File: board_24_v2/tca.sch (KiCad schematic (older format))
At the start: 26 parts, among them IC1 ATMEGA328-A, P1 CONN_2, P2 CONN_3X2, U1 SD_CARD, U2 LD1117S33, Y1 RESONATEUR

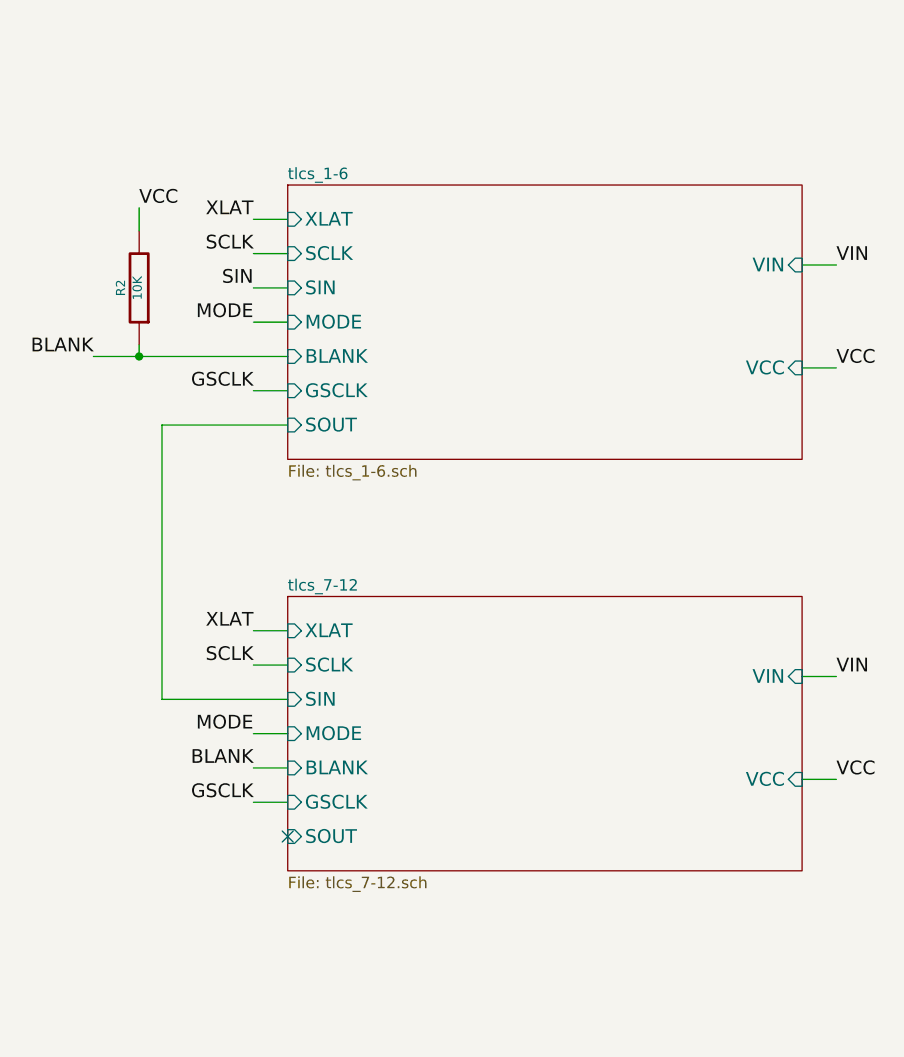
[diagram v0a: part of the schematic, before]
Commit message: Made board_24_v2 which uses PCB-mounted LED sockets and updated various issues on board_96 as well. These PCBs were ordered around 7/1/14.
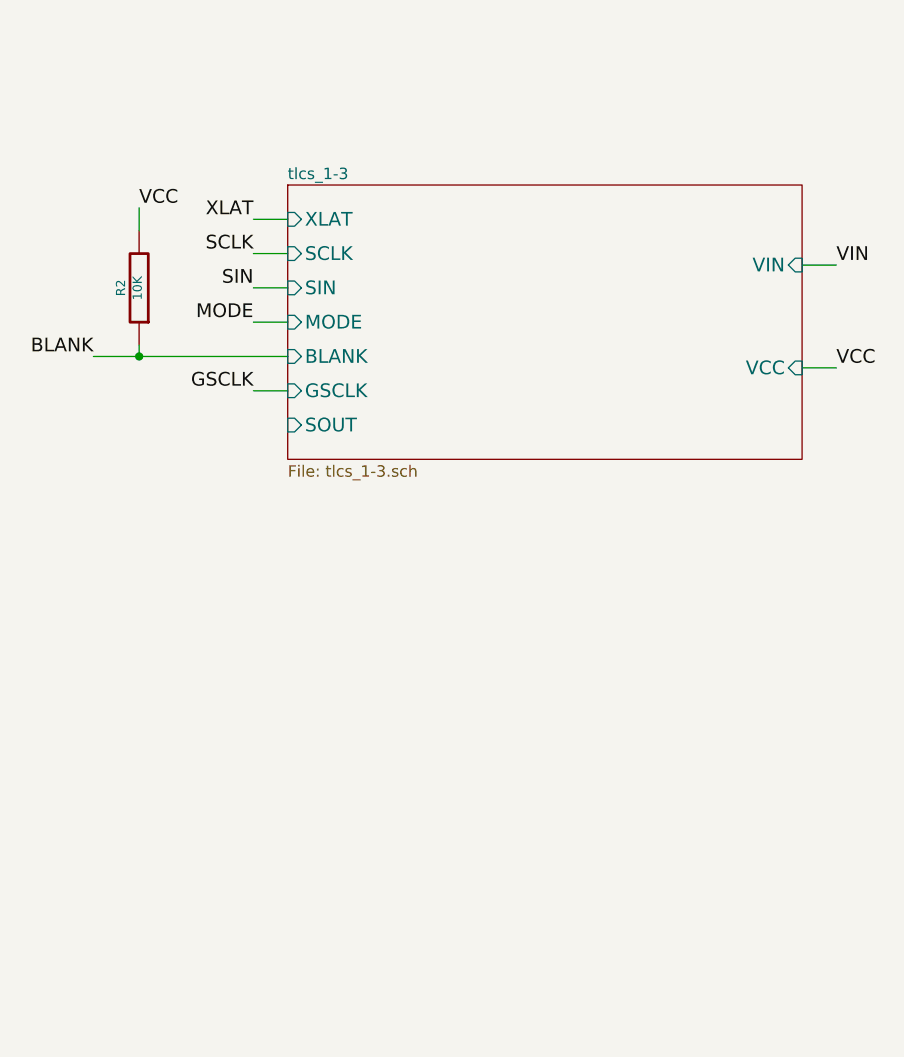
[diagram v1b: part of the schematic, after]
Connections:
- no-connect marks 11 -> 10
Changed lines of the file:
@@
 $Descr USLetter 11000 8500
 encoding utf-8
-Sheet 1 3
+Sheet 1 2
 Title ""
-Date "25 jun 2014"
+Date "27 jun 2014"
 Rev ""
 Comp ""
@@
 S 6800 2450 2250 1200
 U 5362FF20
-F0 "tlcs_1-6" 50
-F1 "tlcs_1-6.sch" 50
+F0 "tlcs_1-3" 50
+F1 "tlcs_1-3.sch" 50
 F2 "XLAT" I L 6800 2600 60
 F3 "SCLK" I L 6800 2750 60
@@
 Text Label 5950 3200 2    60   ~ 0
 BLANK
-Text Label 6650 4400 2    60   ~ 0
-XLAT
-Text Label 6650 4550 2    60   ~ 0
-SCLK
-Text Label 6650 4850 2    60   ~ 0
-MODE
-Text Label 6650 5150 2    60   ~ 0
-GSCLK
-Text Label 9200 4600 0    60   ~ 0
-VIN
-Text Label 9200 5050 0    60   ~ 0
-VCC
-Text Label 6650 5000 2    60   ~ 0
-BLANK
-NoConn ~ 6800 5300
-$Sheet
-S 6800 4250 2250 1200
-U 53633D51
-F0 "tlcs_7-12" 50
-F1 "tlcs_7-12.sch" 50
-F2 "XLAT" I L 6800 4400 60
-F3 "SCLK" I L 6800 4550 60
-F4 "SIN" I L 6800 4700 60
-F5 "MODE" I L 6800 4850 60
-F6 "BLANK" I L 6800 5000 60
-F7 "GSCLK" I L 6800 5150 60
-F8 "VIN" I R 9050 4600 60
-F9 "VCC" I R 9050 5050 60
-F10 "SOUT" I L 6800 5300 60
-$EndSheet
 $Comp
 L INDUCTOR L1
@@
 	9050 3250 9200 3250
 Wire Wire Line
-	6650 5000 6800 5000
-Wire Wire Line
-	6800 4400 6650 4400
-Wire Wire Line
-	6800 4550 6650 4550
-Wire Wire Line
-	6250 4700 6800 4700
-Wire Wire Line
-	6800 4850 6650 4850
-Wire Wire Line
-	6800 5150 6650 5150
-Wire Wire Line
-	9050 4600 9200 4600
-Wire Wire Line
-	9050 5050 9200 5050
-Wire Wire Line
-	6800 3500 6250 3500
-Wire Wire Line
-	6250 3500 6250 4700
-Wire Wire Line
 	6150 3150 6150 3200
